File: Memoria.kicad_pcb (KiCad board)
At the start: 2 copper layers, 242.9 x 96.6 mm, 136 parts, among them J1 RGB Breakout, J2 Hull LED Breakout, U1 PRTR5V0U2X, U2 ATmega32U4-MUR, Y1 16MHz

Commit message: the final final pass
silkscreen art, added 470 resistor, changed 1uF capacitor in BOM
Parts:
- removed the G*** at (146.5, -50.2)
- added G***: LOGO, LOGO, F.Cu at (174.8, 89.7)
- added G***: LOGO, LOGO, F.Cu at (176.2, 80.3)
- added R21: 470, Resistor_SMD:R_0805_2012Metric, B.Cu at (93.6, 58.0)
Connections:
- U2 pad 39: rgbLED -> F4
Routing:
- net rgbLED: track 186.7 -> 107.1 mm, vias 8 -> 2
- net F4: track 0.00 -> 77.9 mm, vias 0 -> 4
- net GND: track 355.5 -> 328.1 mm, vias 41 -> 21

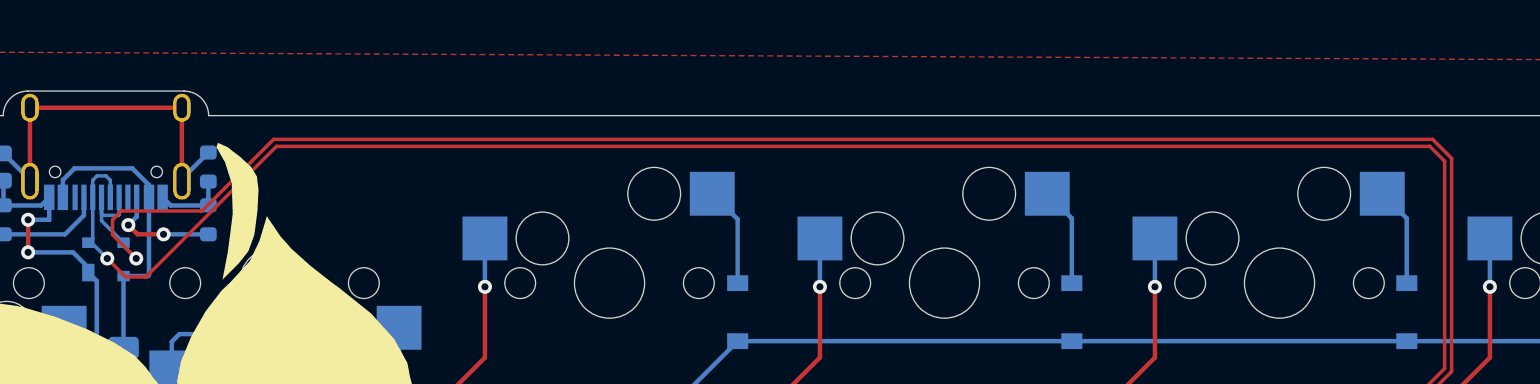
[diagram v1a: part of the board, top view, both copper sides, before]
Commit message: added termination resistors
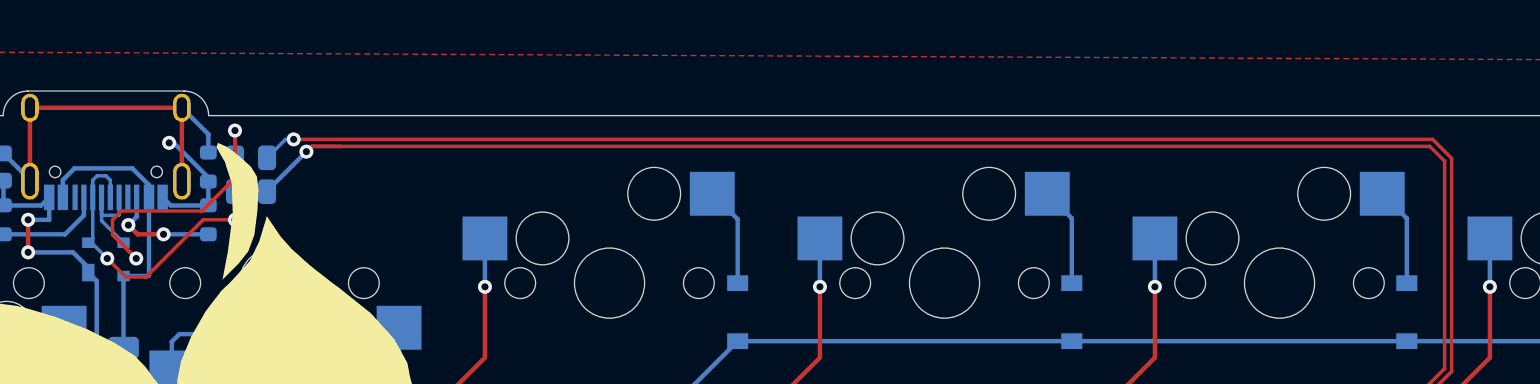
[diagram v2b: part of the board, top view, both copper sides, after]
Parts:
- added R6: 22, Resistor_SMD:R_0805_2012Metric, B.Cu at (60.6, 31.0)
- added R7: 22, Resistor_SMD:R_0805_2012Metric, B.Cu at (60.6, 32.9)
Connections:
- U2 pad 3: D- -> Net-(R7-Pad2)
- U2 pad 4: D+ -> Net-(R6-Pad2)
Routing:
- net Net-(R7-Pad2): track 0.00 -> 153.7 mm, vias 0 -> 2
- net D-: track 170.9 -> 17.9 mm
- net Net-(R6-Pad2): track 0.00 -> 151.7 mm, vias 0 -> 2
- net D+: track 172.0 -> 22.2 mm
- net GND: track 328.1 -> 331.4 mm, vias 21 -> 22
- net Earth: track 21.5 -> 22.5 mm

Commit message: updated revision number
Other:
- board text added: "rev1.1"
- board text removed: "rev1.0"
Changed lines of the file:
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@@
     (effects (font (size 1 1) (thickness 0.15)) (justify mirror))
   )
-  (gr_text "rev1.0" (at 263.25 122) (layer "B.SilkS")
+  (gr_text "rev1.1" (at 263.25 122) (layer "B.SilkS")
     (effects (font (size 1 1) (thickness 0.15)) (justify mirror))
   )
